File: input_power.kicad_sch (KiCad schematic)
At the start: 11 parts

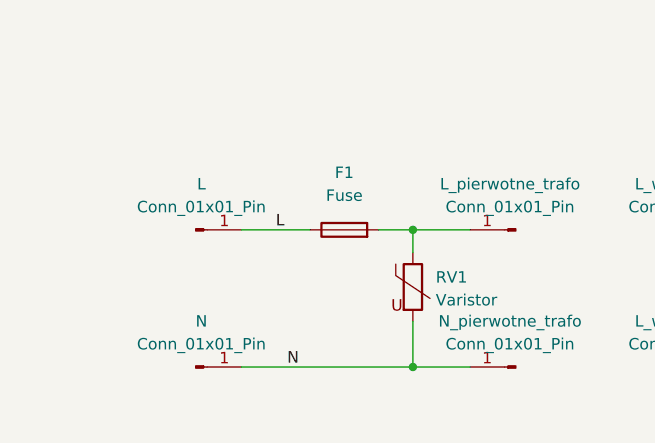
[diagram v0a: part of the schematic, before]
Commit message: zmiana sekcji zasilania digital oraz drivera
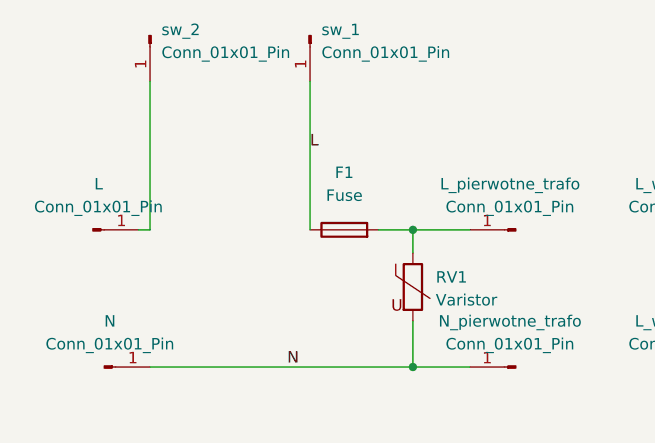
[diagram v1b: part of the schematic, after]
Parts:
- added sw_1, sw_2: Conn_01x01_Pin, symbol Connector:Conn_01x01_Pin
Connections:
- net L: now also sw_1.1 (Pin_1); no longer L.1 (Pin_1)
- new net: L.1 (Pin_1), sw_2.1 (Pin_1)
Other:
- moved on the sheet: L, N
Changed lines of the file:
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@@
 	(wire
 		(pts
-			(xy 38.1 53.34) (xy 57.15 53.34)
+			(xy 27.94 53.34) (xy 57.15 53.34)
 		)
 		(stroke
@@
 	(wire
 		(pts
-			(xy 38.1 38.1) (xy 45.72 38.1)
-		)
-		(stroke
-			(width 0)
-			(type default)
-		)
-	)
-	(wire
-		(pts
 			(xy 140.97 53.34) (xy 127 53.34)
 		)
@@
 	(wire
 		(pts
+			(xy 27.94 38.1) (xy 27.94 21.59)
+		)
+		(stroke
+			(width 0)
+			(type default)
+		)
+	)
+	(wire
+		(pts
 			(xy 127 41.91) (xy 127 38.1)
 		)
@@
 	(wire
 		(pts
+			(xy 26.67 38.1) (xy 27.94 38.1)
+		)
+		(stroke
+			(width 0)
+			(type default)
+		)
+	)
+	(wire
+		(pts
 			(xy 140.97 49.53) (xy 140.97 53.34)
 		)
@@
 	(wire
 		(pts
+			(xy 45.72 21.59) (xy 45.72 38.1)
+		)
+		(stroke
+			(width 0)
+			(type default)
+		)
+	)
+	(wire
+		(pts
 			(xy 57.15 48.26) (xy 57.15 53.34)
 		)
@@
 	)
 	(label "L"
-		(at 41.91 38.1 0)
+		(at 45.72 29.21 0)
 		(effects
 			(font
@@
 	(symbol
 		(lib_id "Connector:Conn_01x01_Pin")
-		(at 33.02 53.34 0)
+		(at 22.86 53.34 0)
 		(unit 1)
 		(exclude_from_sim no)
@@
 		(fields_autoplaced yes)
 		(property "Reference" "N"
-			(at 33.655 48.26 0)
+			(at 23.495 48.26 0)
 			(effects
 				(font
@@
 		)
 		(property "Value" "Conn_01x01_Pin"
-			(at 33.655 50.8 0)
+			(at 23.495 50.8 0)
 			(effects
 				(font
@@
 		)
 		(property "Footprint" ""
-			(at 33.02 53.34 0)
+			(at 22.86 53.34 0)
 			(effects
 				(font
@@
 		)
 		(property "Datasheet" "~"
-			(at 33.02 53.34 0)
+			(at 22.86 53.34 0)
 			(effects
 				(font
@@
 		)
 		(property "Description" "Generic connector, single row, 01x01, script generated"
-			(at 33.02 53.34 0)
+			(at 22.86 53.34 0)
 			(effects
 				(font
@@
 	(symbol
 		(lib_id "Connector:Conn_01x01_Pin")
-		(at 33.02 38.1 0)
+		(at 21.59 38.1 0)
 		(unit 1)
 		(exclude_from_sim no)
@@
 		(fields_autoplaced yes)
 		(property "Reference" "L"
-			(at 33.655 33.02 0)
+			(at 22.225 33.02 0)
 			(effects
 				(font
@@
 		)
 		(property "Value" "Conn_01x01_Pin"
-			(at 33.655 35.56 0)
+			(at 22.225 35.56 0)
 			(effects
 				(font
@@
 		)
 		(property "Footprint" ""
-			(at 33.02 38.1 0)
+			(at 21.59 38.1 0)
 			(effects
 				(font
@@
 		)
 		(property "Datasheet" "~"
-			(at 33.02 38.1 0)
+			(at 21.59 38.1 0)
 			(effects
 				(font
@@
 		)
 		(property "Description" "Generic connector, single row, 01x01, script generated"
-			(at 33.02 38.1 0)
+			(at 21.59 38.1 0)
 			(effects
 				(font
@@
 	)
 	(symbol
+		(lib_id "Connector:Conn_01x01_Pin")
+		(at 45.72 16.51 270)
+		(unit 1)
+		(exclude_from_sim no)
+		(in_bom yes)
+		(on_board yes)
+		(dnp no)
+		(fields_autoplaced yes)
+		(property "Reference" "sw_1"
+			(at 46.99 15.8749 90)
+			(effects
+				(font
+					(size 1.27 1.27)
+				)
+				(justify left)
+			)
+		)
+		(property "Value" "Conn_01x01_Pin"
+			(at 46.99 18.4149 90)
+			(effects
+				(font
+					(size 1.27 1.27)
+				)
+				(justify left)
+			)
+		)
+		(property "Footprint" ""
+			(at 45.72 16.51 0)
+			(effects
+				(font
+					(size 1.27 1.27)
+				)
+				(hide yes)
+			)
+		)
+		(property "Datasheet" "~"
+			(at 45.72 16.51 0)
+			(effects
+				(font
+					(size 1.27 1.27)
+				)
+				(hide yes)
+			)
+		)
+		(property "Description" "Generic connector, single row, 01x01, script generated"
+			(at 45.72 16.51 0)
+			(effects
+				(font
+					(size 1.27 1.27)
+				)
+				(hide yes)
+			)
+		)
+		(pin "1"
+		)
+		(instances
+			(project "zasilacz_projekt_kompetencyjny"
+				(path "/e9ad3936-200e-4b7c-85fb-533ca6ea54fd/4c5d3d73-d998-497c-8772-3ed3fa3bb913"
+					(reference "sw_1")
+					(unit 1)
+				)
+			)
+		)
+	)
+	(symbol
 		(lib_id "Diode_Bridge:GBU8B")
 		(at 107.95 45.72 0)
@@
 					(unit 1)
 				)
+			)
+		)
+	)
+	(symbol
+		(lib_id "Connector:Conn_01x01_Pin")
+		(at 27.94 16.51 270)
+		(unit 1)
+		(exclude_from_sim no)
+		(in_bom yes)
+		(on_board yes)
+		(dnp no)
+		(fields_autoplaced yes)
+		(property "Reference" "sw_2"
+			(at 29.21 15.8749 90)
+			(effects
+				(font
+					(size 1.27 1.27)
+				)
+				(justify left)
+			)
+		)
+		(property "Value" "Conn_01x01_Pin"
+			(at 29.21 18.4149 90)
+			(effects
+				(font
+					(size 1.27 1.27)
+				)
+				(justify left)
+			)
+		)
+		(property "Footprint" ""
+			(at 27.94 16.51 0)
+			(effects
+				(font
+					(size 1.27 1.27)
+				)
+				(hide yes)
+			)
+		)
+		(property "Datasheet" "~"
+			(at 27.94 16.51 0)
+			(effects
+				(font
+					(size 1.27 1.27)
+				)
+				(hide yes)
+			)
+		)
+		(property "Description" "Generic connector, single row, 01x01, script generated"
+			(at 27.94 16.51 0)
+			(effects
+				(font
+					(size 1.27 1.27)
+				)
+				(hide yes)
+			)
+		)
+		(pin "1"
+		)
+		(instances
+			(project "zasilacz_projekt_kompetencyjny"
+				(path "/e9ad3936-200e-4b7c-85fb-533ca6ea54fd/4c5d3d73-d998-497c-8772-3ed3fa3bb913"
+					(reference "sw_2")
+					(unit 1)
+				)

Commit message: dodanie footprintów w sekcji input power
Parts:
- C1: footprint (none) -> Capacitor_THT:CP_Radial_D35.0mm_P10.00mm_SnapIn
- C2: footprint (none) -> Capacitor_THT:C_Disc_D10.0mm_W2.5mm_P5.00mm
- F1: footprint (none) -> Fuseholder_Cylinder-5x20mm_Schurter_0031_8201_Horizontal_Open
- L, N, sw_1, sw_2: footprint (none) -> Connector_Wire:SolderWire-1.5sqmm_1x01_D1.7mm_OD3mm
- L_pierwotne_trafo, L_wtórne_trafo, N_pierwotne_trafo: footprint (none) -> Connector_Wire:SolderWire-2.5sqmm_1x01_D2.4mm_OD4.4mm
- RV1: footprint (none) -> Varistor:RV_Disc_D21.5mm_W4.3mm_P10mm
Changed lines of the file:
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@@
 			)
 		)
-		(property "Footprint" ""
+		(property "Footprint" "Capacitor_THT:C_Disc_D10.0mm_W2.5mm_P5.00mm"
 			(at 141.9352 49.53 0)
 			(hide yes)
@@
 			)
 		)
-		(property "Footprint" ""
+		(property "Footprint" "Fuseholder_Cylinder-5x20mm_Schurter_0031_8201_Horizontal_Open"
 			(at 49.53 39.878 90)
 			(hide yes)
@@
 			)
 		)
-		(property "Footprint" ""
+		(property "Footprint" "Connector_Wire:SolderWire-1.5sqmm_1x01_D1.7mm_OD3mm"
 			(at 22.86 53.34 0)
 			(hide yes)
@@
 			)
 		)
-		(property "Footprint" ""
+		(property "Footprint" "Connector_Wire:SolderWire-1.5sqmm_1x01_D1.7mm_OD3mm"
 			(at 21.59 38.1 0)
 			(hide yes)
@@
 			)
 		)
-		(property "Footprint" ""
+		(property "Footprint" "Connector_Wire:SolderWire-1.5sqmm_1x01_D1.7mm_OD3mm"
 			(at 45.72 16.51 0)
 			(hide yes)
@@
 			)
 		)
-		(property "Footprint" ""
+		(property "Footprint" "Connector_Wire:SolderWire-2.5sqmm_1x01_D2.4mm_OD4.4mm"
 			(at 68.58 38.1 0)
 			(hide yes)
@@
 			)
 		)
-		(property "Footprint" ""
+		(property "Footprint" "Connector_Wire:SolderWire-2.5sqmm_1x01_D2.4mm_OD4.4mm"
 			(at 68.58 53.34 0)
 			(hide yes)
@@
 			)
 		)
-		(property "Footprint" ""
+		(property "Footprint" "Varistor:RV_Disc_D21.5mm_W4.3mm_P10mm"
 			(at 55.372 44.45 90)
 			(hide yes)
@@
 			)
 		)
-		(property "Footprint" ""
+		(property "Footprint" "Capacitor_THT:CP_Radial_D35.0mm_P10.00mm_SnapIn"
 			(at 127.9652 49.53 0)
 			(hide yes)
@@
 			)
 		)
-		(property "Footprint" ""
+		(property "Footprint" "Connector_Wire:SolderWire-2.5sqmm_1x01_D2.4mm_OD4.4mm"
 			(at 87.63 38.1 0)
 			(hide yes)
@@
 			)
 		)
-		(property "Footprint" ""
+		(property "Footprint" "Connector_Wire:SolderWire-1.5sqmm_1x01_D1.7mm_OD3mm"
 			(at 27.94 16.51 0)
 			(hide yes)
@@
 			)
 		)
-		(property "Footprint" ""
+		(property "Footprint" "Connector_Wire:SolderWire-2.5sqmm_1x01_D2.4mm_OD4.4mm"
 			(at 87.63 53.34 0)
 			(hide yes)

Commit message: Dodanie brakującego połączenia do przycisków enkoderów
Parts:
- renumbered L to L3, L_pierwotne_trafo to L_pierwotne_trafo1, L_wtórne_trafo to L_wtórne_trafo1, L_wtórne_trafo to L_wtórne_trafo2, N to N1, N_pierwotne_trafo to N_pierwotne_trafo1
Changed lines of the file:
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@@
 		(dnp no)
 		(fields_autoplaced yes)
-		(property "Reference" "N"
+		(property "Reference" "N1"
 			(at 23.495 48.26 0)
 			(show_name no)
@@
 			(project "zasilacz_projekt_kompetencyjny"
 				(path "/e9ad3936-200e-4b7c-85fb-533ca6ea54fd/4c5d3d73-d998-497c-8772-3ed3fa3bb913"
-					(reference "N")
+					(reference "N1")
 					(unit 1)
 				)
@@
 		(dnp no)
 		(fields_autoplaced yes)
-		(property "Reference" "L"
+		(property "Reference" "L3"
 			(at 22.225 33.02 0)
 			(show_name no)
@@
 			(project "zasilacz_projekt_kompetencyjny"
 				(path "/e9ad3936-200e-4b7c-85fb-533ca6ea54fd/4c5d3d73-d998-497c-8772-3ed3fa3bb913"
-					(reference "L")
+					(reference "L3")
 					(unit 1)
 				)
@@
 		(dnp no)
 		(fields_autoplaced yes)
-		(property "Reference" "L_pierwotne_trafo"
+		(property "Reference" "L_pierwotne_trafo1"
 			(at 67.945 33.02 0)
 			(show_name no)
@@
 			(project "zasilacz_projekt_kompetencyjny"
 				(path "/e9ad3936-200e-4b7c-85fb-533ca6ea54fd/4c5d3d73-d998-497c-8772-3ed3fa3bb913"
-					(reference "L_pierwotne_trafo")
+					(reference "L_pierwotne_trafo1")
 					(unit 1)
 				)
@@
 		(dnp no)
 		(fields_autoplaced yes)
-		(property "Reference" "N_pierwotne_trafo"
+		(property "Reference" "N_pierwotne_trafo1"
 			(at 67.945 48.26 0)
 			(show_name no)
@@
 			(project "zasilacz_projekt_kompetencyjny"
 				(path "/e9ad3936-200e-4b7c-85fb-533ca6ea54fd/4c5d3d73-d998-497c-8772-3ed3fa3bb913"
-					(reference "N_pierwotne_trafo")
+					(reference "N_pierwotne_trafo1")
 					(unit 1)
 				)
@@
 		(dnp no)
 		(fields_autoplaced yes)
-		(property "Reference" "L_wtórne_trafo"
+		(property "Reference" "L_wtórne_trafo1"
 			(at 88.265 33.02 0)
 			(show_name no)
@@
 			(project "zasilacz_projekt_kompetencyjny"
 				(path "/e9ad3936-200e-4b7c-85fb-533ca6ea54fd/4c5d3d73-d998-497c-8772-3ed3fa3bb913"
-					(reference "L_wtórne_trafo")
+					(reference "L_wtórne_trafo1")
 					(unit 1)
 				)
@@
 		(dnp no)
 		(fields_autoplaced yes)
-		(property "Reference" "L_wtórne_trafo"
+		(property "Reference" "L_wtórne_trafo2"
 			(at 88.265 48.26 0)
 			(show_name no)
@@
 			(project "zasilacz_projekt_kompetencyjny"
 				(path "/e9ad3936-200e-4b7c-85fb-533ca6ea54fd/4c5d3d73-d998-497c-8772-3ed3fa3bb913"
-					(reference "L_wtórne_trafo")
-					(unit 1)
-				)
+					(reference "L_wtórne_trafo2")
+					(unit 1)
+				)

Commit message: Przydzielenie brakujących footprintów dla części cyfrowej oprócz enkoderów
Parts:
- F1: footprint Fuseholder_Cylinder-5x20mm_Schurter_0031_8201_Horizontal_Open -> Fuse:Fuseholder_Cylinder-5x20mm_Schurter_0031_8201_Horizontal_Open
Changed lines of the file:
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@@
 			)
 		)
-		(property "Footprint" "Fuseholder_Cylinder-5x20mm_Schurter_0031_8201_Horizontal_Open"
+		(property "Footprint" "Fuse:Fuseholder_Cylinder-5x20mm_Schurter_0031_8201_Horizontal_Open"
 			(at 49.53 39.878 90)
 			(hide yes)

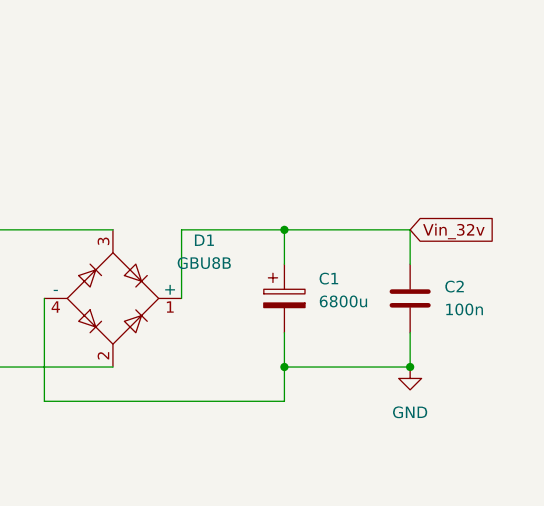
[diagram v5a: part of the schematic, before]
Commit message: dodanie wentylatora, drobne zmiany wartości elementów
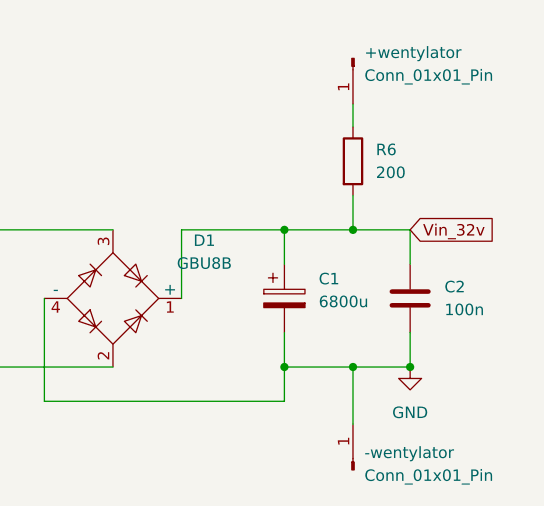
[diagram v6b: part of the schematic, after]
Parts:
- added +wentylator, -wentylator: Conn_01x01_Pin, Connector_Wire:SolderWire-1.5sqmm_1x01_D1.7mm_OD3mm, symbol Connector:Conn_01x01_Pin
- added R6: 200, Resistor_THT:R_Axial_DIN0411_L9.9mm_D3.6mm_P15.24mm_Horizontal, symbol Device:R
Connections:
- net GND: now also -wentylator.1 (Pin_1)
- net Vin_32v: now also R6.2
- new net: +wentylator.1 (Pin_1), R6.1

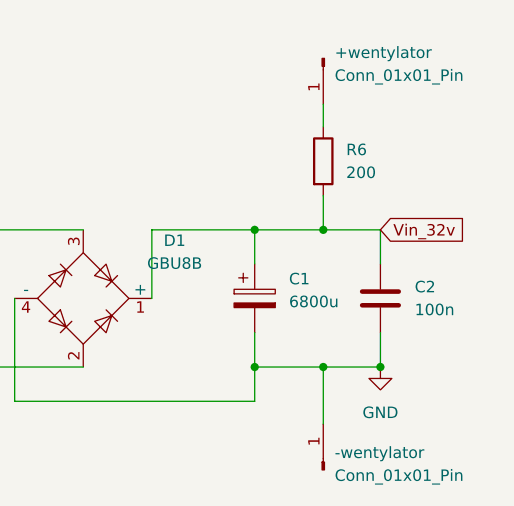
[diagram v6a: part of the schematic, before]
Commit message: Narysowanie części cyfrowej płytki, części zasialania przetwornicy głównej oraz zasilania części cyfrowej, do dokończenia połączenia mas oraz zasilań
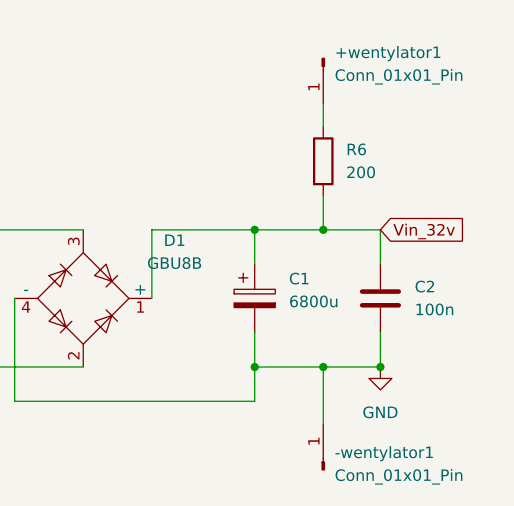
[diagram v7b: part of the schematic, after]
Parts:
- renumbered +wentylator to +wentylator1, -wentylator to -wentylator1
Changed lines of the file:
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@@
 		(dnp no)
 		(fields_autoplaced yes)
-		(property "Reference" "-wentylator"
+		(property "Reference" "-wentylator1"
 			(at 135.89 62.8649 90)
 			(show_name no)
@@
 			(project "zasilacz_projekt_kompetencyjny"
 				(path "/e9ad3936-200e-4b7c-85fb-533ca6ea54fd/4c5d3d73-d998-497c-8772-3ed3fa3bb913"
-					(reference "-wentylator")
+					(reference "-wentylator1")
 					(unit 1)
 				)
@@
 		(dnp no)
 		(fields_autoplaced yes)
-		(property "Reference" "+wentylator"
+		(property "Reference" "+wentylator1"
 			(at 135.89 18.4149 90)
 			(show_name no)
@@
 			(project "zasilacz_projekt_kompetencyjny"
 				(path "/e9ad3936-200e-4b7c-85fb-533ca6ea54fd/4c5d3d73-d998-497c-8772-3ed3fa3bb913"
-					(reference "+wentylator")
+					(reference "+wentylator1")
 					(unit 1)
 				)
@@
 		)
 	)
-	(embedded_fonts no)
 )
